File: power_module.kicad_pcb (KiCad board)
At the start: 4 copper layers, 95 x 66 mm, 71 parts, among them J1 USB_C_PD, J2 OUTPUT, J3 I2C_BREAKOUT, Q1 DUAL_N_FET, Q2 DUAL_N_FET, Q3 DUAL_N_FET, Q4 DUAL_N_FET, SW1 ON_OFF, U1 BQ7692003, U2 CH224K, U3 BQ24650, U4 LM5176PWPR

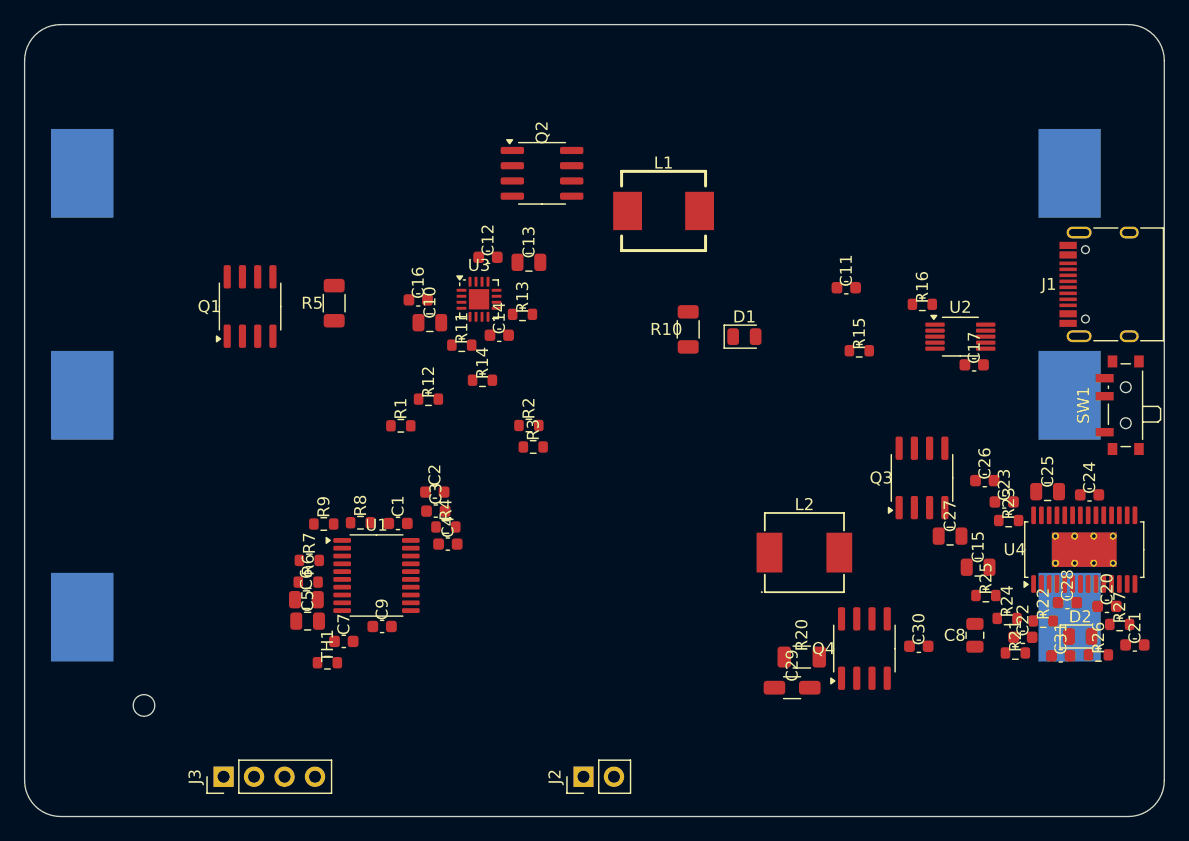
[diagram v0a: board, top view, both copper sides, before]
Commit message: PCB: autoroute + refill_zones pass
Post-tuning autoplacer state autoroute via freerouting with the
GND-last layer order ([F.Cu, B.Cu, In2.Cu, In1.Cu]) — 593 tracks,
84 vias, 149.5s. Refilled both zones (GND on In1.Cu, BAT+ on In2.Cu).

DRC: 358 errors → 54 errors post-refill.

Also added 6 intra-IC same-net pad bridges (0.3-0.5 mm narrow):
U4.2/3 BAT+, U4.12/13 V12_OUT, U1.9/10 BAT+, Q3.7/8 BAT+,
Q2.5/6 BQ_PH, Q2.7/8 USB_VBUS.

Pending: BAT1 vias (B.Cu↔In1.Cu bridge for 10 of 20 unconnects),
hand-fix U3/U4 remaining 10 unconnects, final DRC verify.

Co-Authored-By: Claude Opus 4.7 <noreply@anthropic.com>
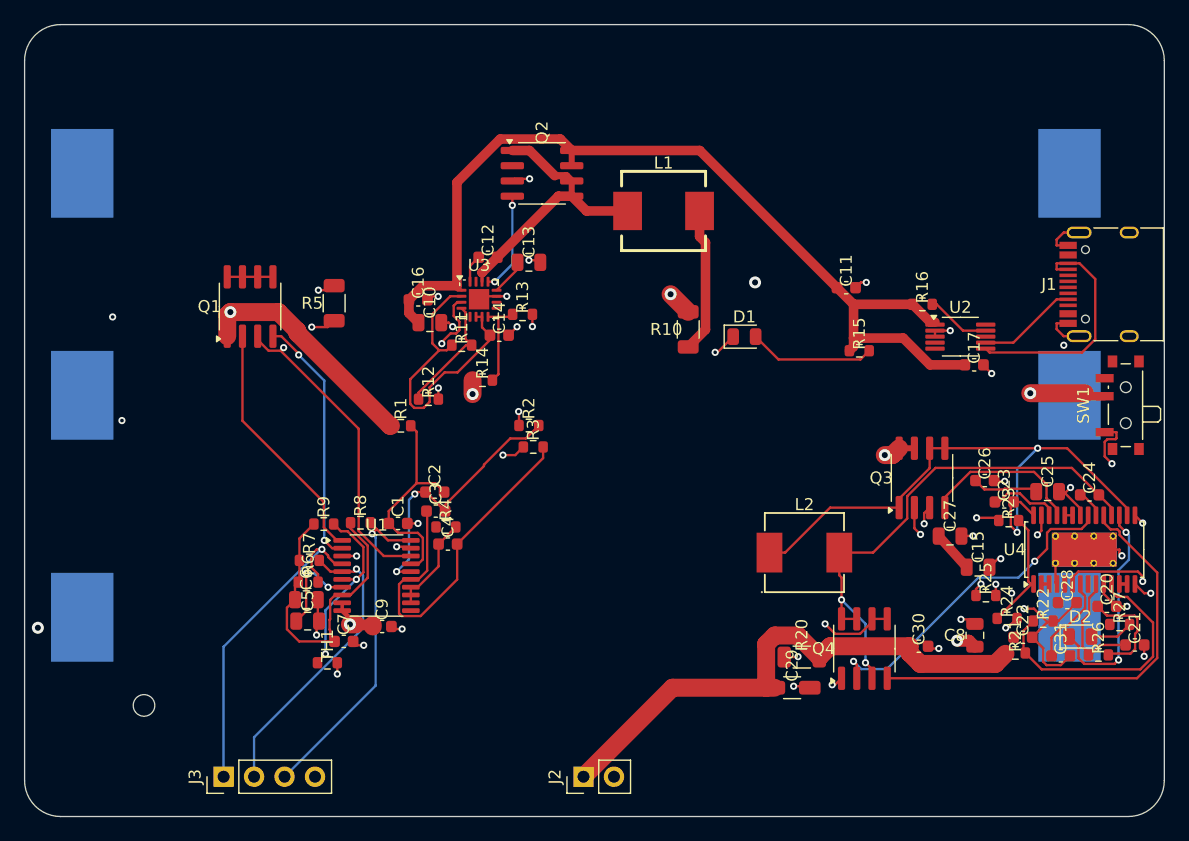
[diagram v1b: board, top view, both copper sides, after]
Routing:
- net CELL1_TOP: track 0.00 -> 103.6 mm, vias 0 -> 3
- net BAT-: track 0.00 -> 94.3 mm, vias 0 -> 2
- net CELL2_TOP: track 0.00 -> 93.2 mm, vias 0 -> 3
- net USB_VBUS: track 0.00 -> 79.2 mm
- net GND: track 0.00 -> 71.1 mm, vias 0 -> 35
- net BB_SW1: track 0.00 -> 50.2 mm, vias 0 -> 2
- net V12_OUT: track 0.00 -> 46.0 mm
- net BB_SW2: track 0.00 -> 43.2 mm, vias 0 -> 2
- net V12_INT: track 0.00 -> 40.9 mm, vias 0 -> 3
- net BB_HDRV2: track 0.00 -> 37.3 mm
- net SRP: track 0.00 -> 31.0 mm, vias 0 -> 2
- net VC2: track 0.00 -> 30.4 mm
- net BQ_STAT1: track 0.00 -> 30.1 mm, vias 0 -> 2
- net SDA: track 0.00 -> 28.2 mm, vias 0 -> 1
- net ALERT: track 0.00 -> 28.0 mm, vias 0 -> 1
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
